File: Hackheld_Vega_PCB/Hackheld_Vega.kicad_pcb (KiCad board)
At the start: 2 copper layers, 50.5 x 67.1 mm, 35 parts, among them J1 Conn_01x04_Female, J2 Conn_01x03_Female, SW1 SW_Push, SW2 SW_Push, SW3 SW_Push, SW4 SW_Push, SW5 SW_Push, SW6 SW_Push, U1 D1_mini

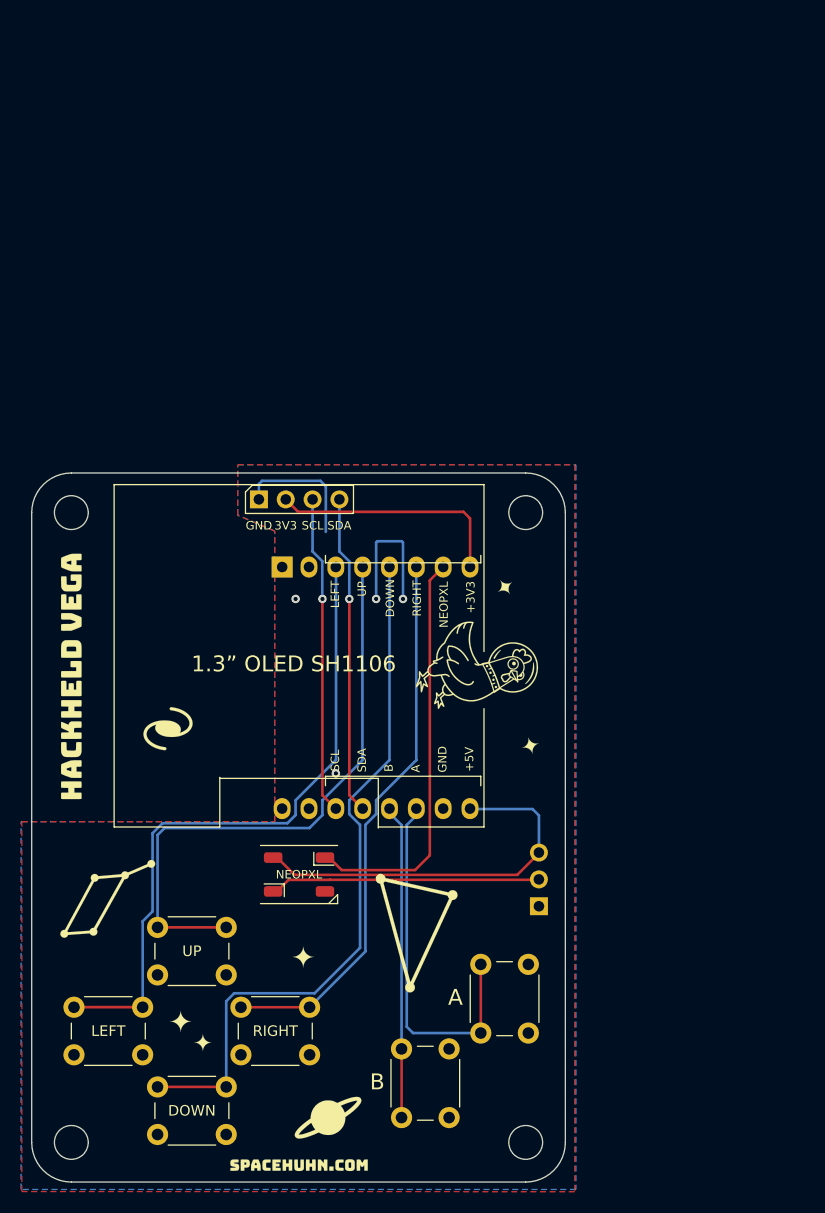
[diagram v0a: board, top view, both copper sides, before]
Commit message: updated netlist, pcb and gerbers to reflect Stefan's change (swapping OLED connector's 3V3 and GND)
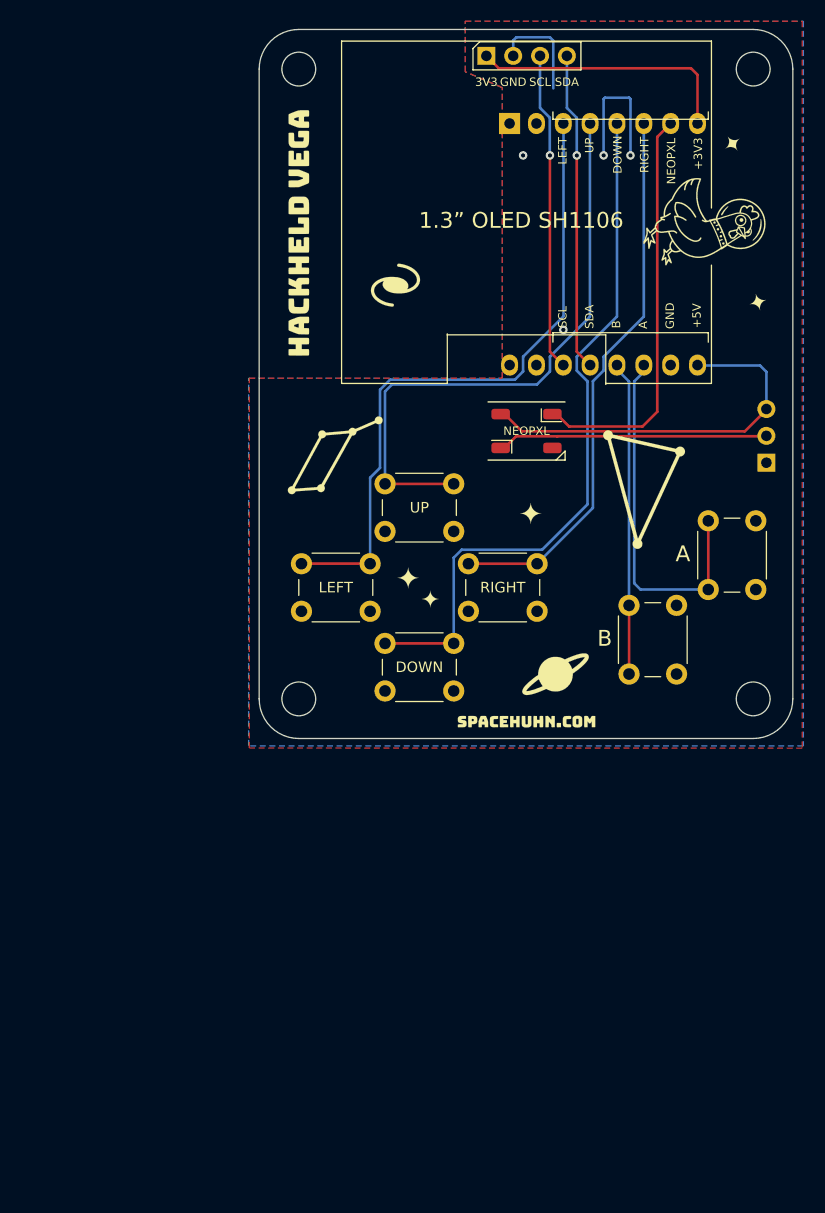
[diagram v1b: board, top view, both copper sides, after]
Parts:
- moved G*** 47.2 mm to (129.2, 108.3)
- moved G*** 47.2 mm to (169.2, 93.8)
- moved G*** 47.2 mm to (147.7, 113.8)
- moved G*** 47.2 mm to (163.8, 86.5)
- moved REF** 47.2 mm to (147.7, 108.1)
- moved D1 47.2 mm to (147.3, 106.0)
- moved G*** 47.2 mm to (147.3, 103.6)
- moved SW2 47.2 mm to (141.8, 118.6)
- moved G*** 47.2 mm to (166.8, 78.8)
- moved G*** 47.2 mm to (138.2, 121.9)
- moved G*** 47.2 mm to (136.1, 119.9)
- moved G*** 47.2 mm to (150.1, 129.0)
- moved G*** 47.2 mm to (125.8, 87.3)
- moved G*** 47.2 mm to (147.3, 133.5)
- moved G*** 47.2 mm to (148.9, 80.7)
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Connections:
- J1 pad 1: GND -> +3V3
- J1 pad 2: +3V3 -> GND
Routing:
- net +3V3: track 22.8 -> 26.0 mm
- net GND: track 28.8 -> 25.7 mm
